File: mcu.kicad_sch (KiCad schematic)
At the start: 14 parts, among them J2 USB_C_Receptacle_USB2.0, J3 SH-6P, SW1 SW_Push, SW2 SW_Push, U3 TJA1051TK-3, U4 STM32G0B1KBU6

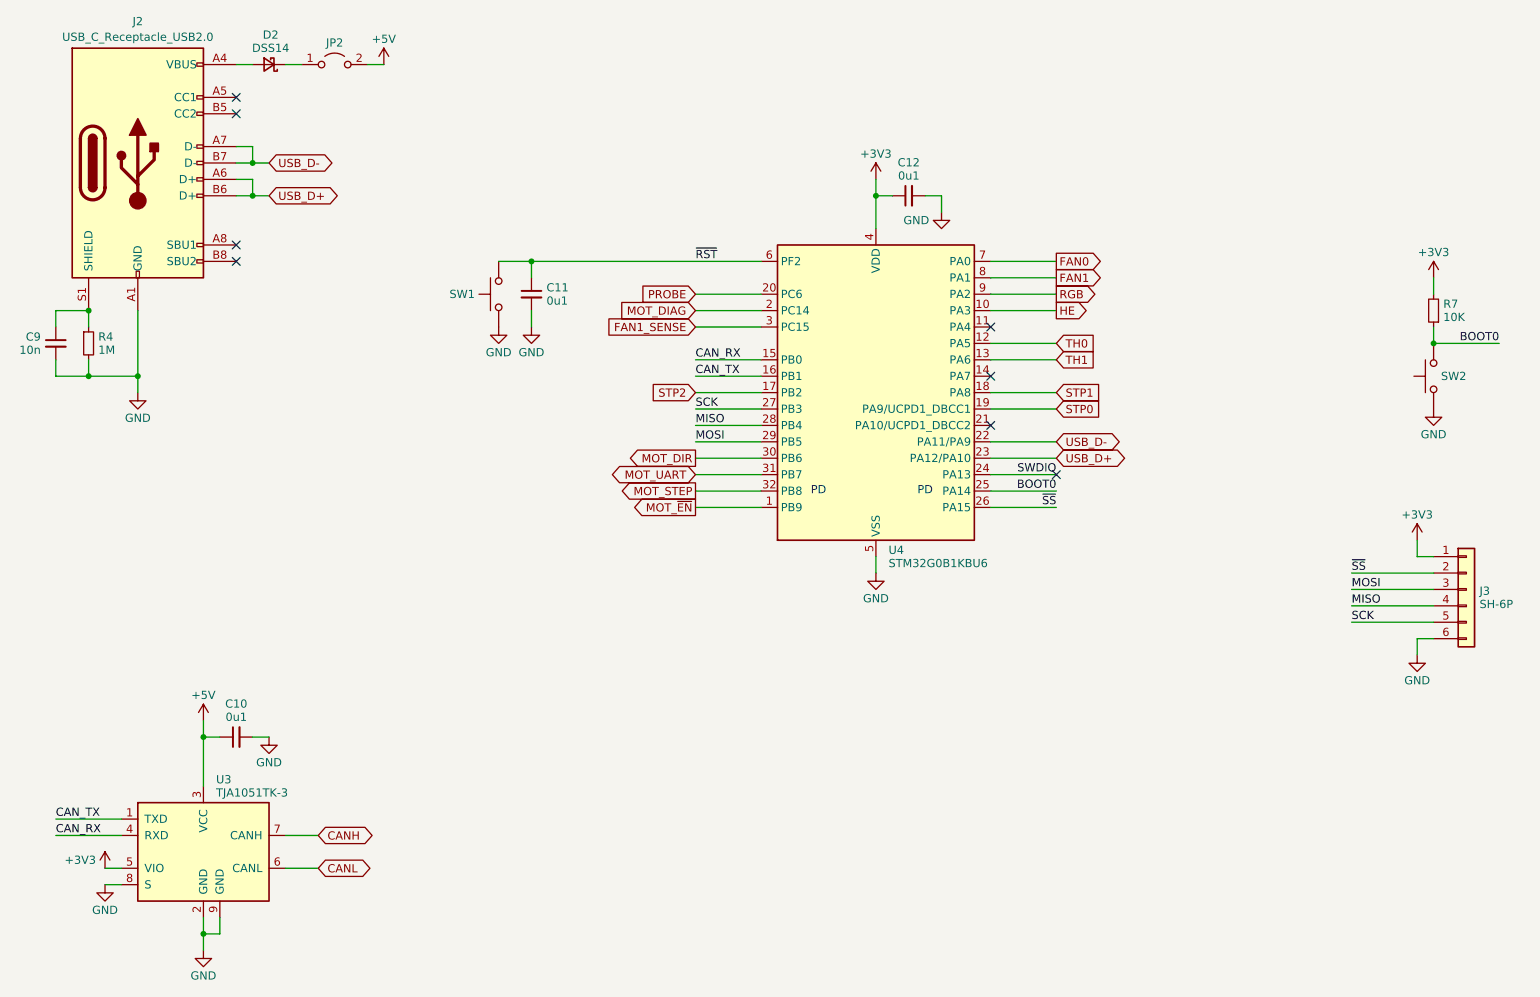
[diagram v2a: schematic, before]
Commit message: Rename fan ports to PCF/HEF
Remove USB series resistors

Add USB clamping diodes
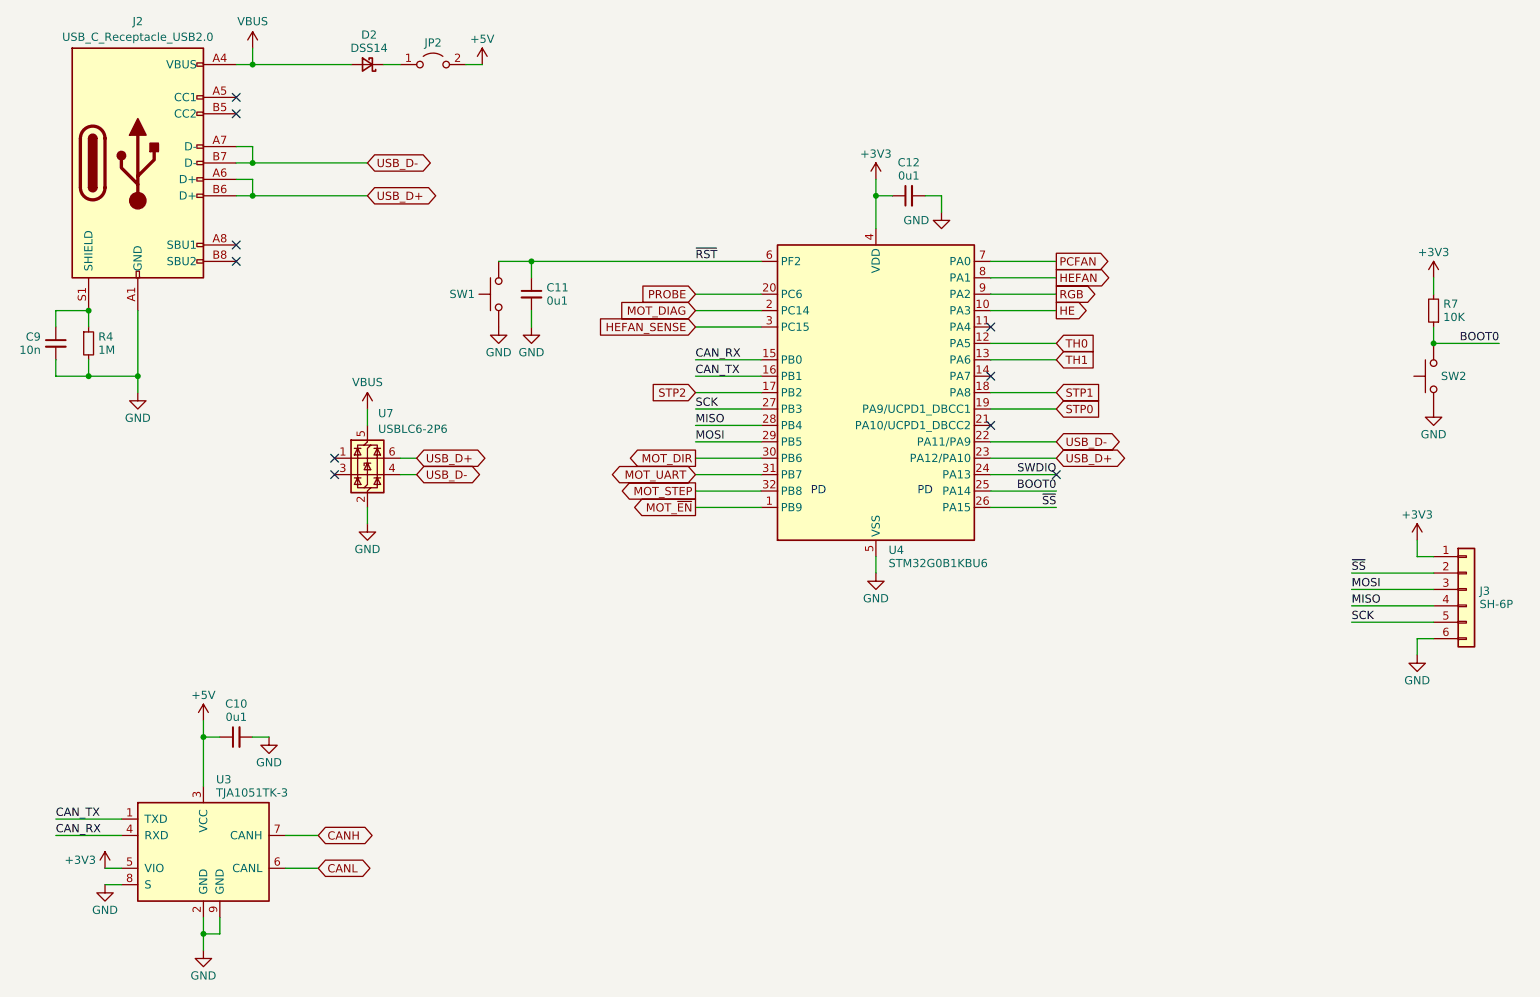
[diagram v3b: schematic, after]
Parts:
- added U7: USBLC6-2P6, Package_TO_SOT_SMD:SOT-666, symbol Power_Protection:USBLC6-2P6
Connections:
- net GND: now also U7.2 (GND)
- net USB_D+: now also U7.6 (I/O1)
- net USB_D-: now also U7.4 (I/O2)
- net VBUS: now reaches D2.2 (A), J2.A4 (VBUS), J2.A9 (VBUS), J2.B4 (VBUS), J2.B9 (VBUS)
- net VBUS: now also U7.5 (VBUS)
- net FAN0 renamed PCFAN
- net FAN1 renamed HEFAN
- net FAN1_SENSE renamed HEFAN_SENSE
- no-connect marks 8 -> 10
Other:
- moved on the sheet: D2, JP2

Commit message: Add USB CC pulldown resistors
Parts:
- removed C10, C11, C12: 0u1, Capacitor_SMD:C_0402_1005Metric, symbol Device:C_Small
- removed C9: 10n, Capacitor_SMD:C_0402_1005Metric, symbol Device:C_Small
- removed D2: DSS14, Diode_SMD:D_SOD-123F, symbol Device:D_Schottky_Small
- removed J2: USB_C_Receptacle_USB2.0, Connector_USB:USB_C_Receptacle_GCT_USB4105-xx-A_16P_TopMnt_Horizontal, symbol Connector:USB_C_Receptacle_USB2.0_16P
- removed J3: SH-6P, Connector_JST:JST_SH_SM06B-SRSS-TB_1x06-1MP_P1.00mm_Horizontal, symbol Connector_Generic:Conn_01x06
- removed JP2: Jumper_2_Open, Connector_PinHeader_2.00mm:PinHeader_1x02_P2.00mm_Vertical, symbol Jumper:Jumper_2_Open
- removed R4: 1M, Resistor_SMD:R_0402_1005Metric, symbol Device:R_Small
- removed R7: 10K, Resistor_SMD:R_0402_1005Metric, symbol Device:R_Small
- removed SW1, SW2: SW_Push, Button_Switch_SMD:SW_SPST_EVQP7A, symbol Switch:SW_Push
- removed U3: TJA1051TK-3, Package_DFN_QFN:DFN-8-1EP_3x3mm_P0.65mm_EP1.55x2.4mm, symbol Interface_CAN_LIN:TJA1051TK-3
- removed U4: STM32G0B1KBU6, Package_DFN_QFN:QFN-32-1EP_5x5mm_P0.5mm_EP3.45x3.45mm, symbol MCU_ST_STM32G0:STM32G0B1KBUx
- removed U7: USBLC6-2P6, Package_TO_SOT_SMD:SOT-666, symbol Power_Protection:USBLC6-2P6
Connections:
- no-connect marks 10 -> 0
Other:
- note removed: "PD"
